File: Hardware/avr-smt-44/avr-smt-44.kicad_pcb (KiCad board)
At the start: 2 copper layers, 25.4 x 72.4 mm, 20 parts, among them J1 AVR-ISP-6, SW1 SW_Push, U1 ATtiny84A-SS

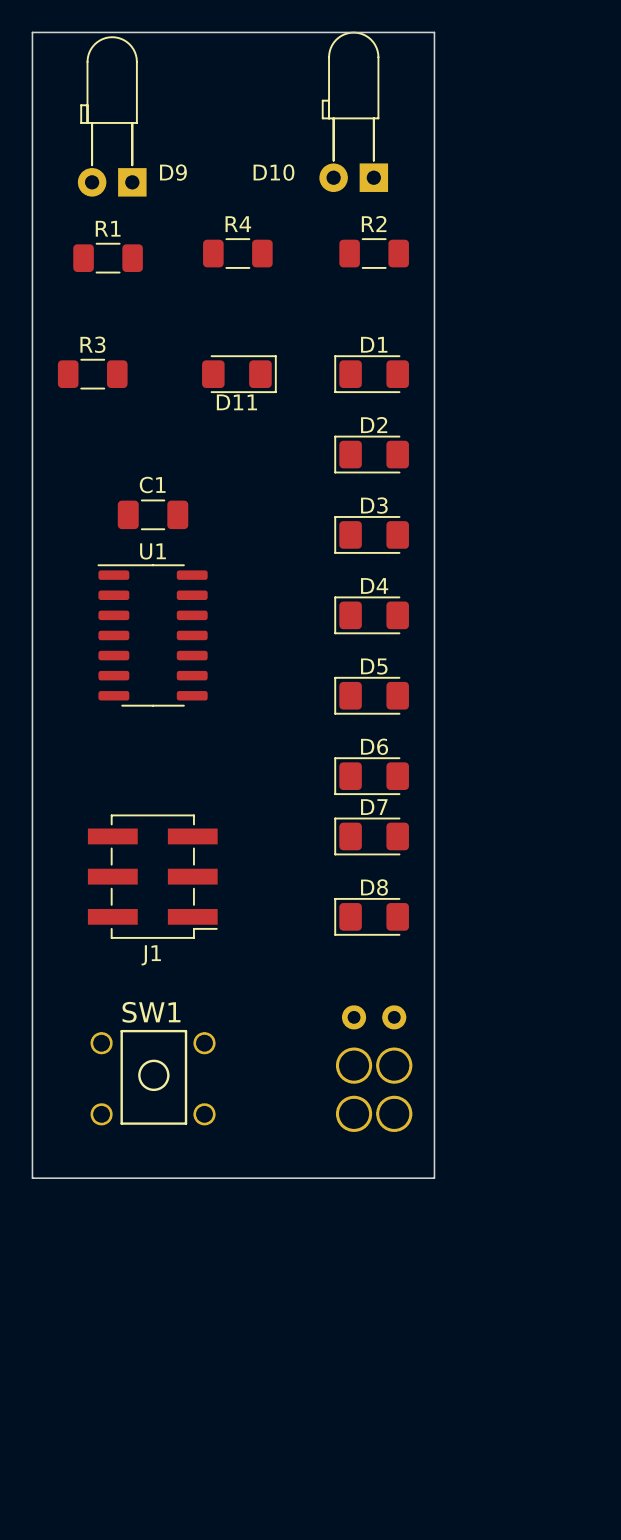
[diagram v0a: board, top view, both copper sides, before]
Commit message: Add series R, re-place
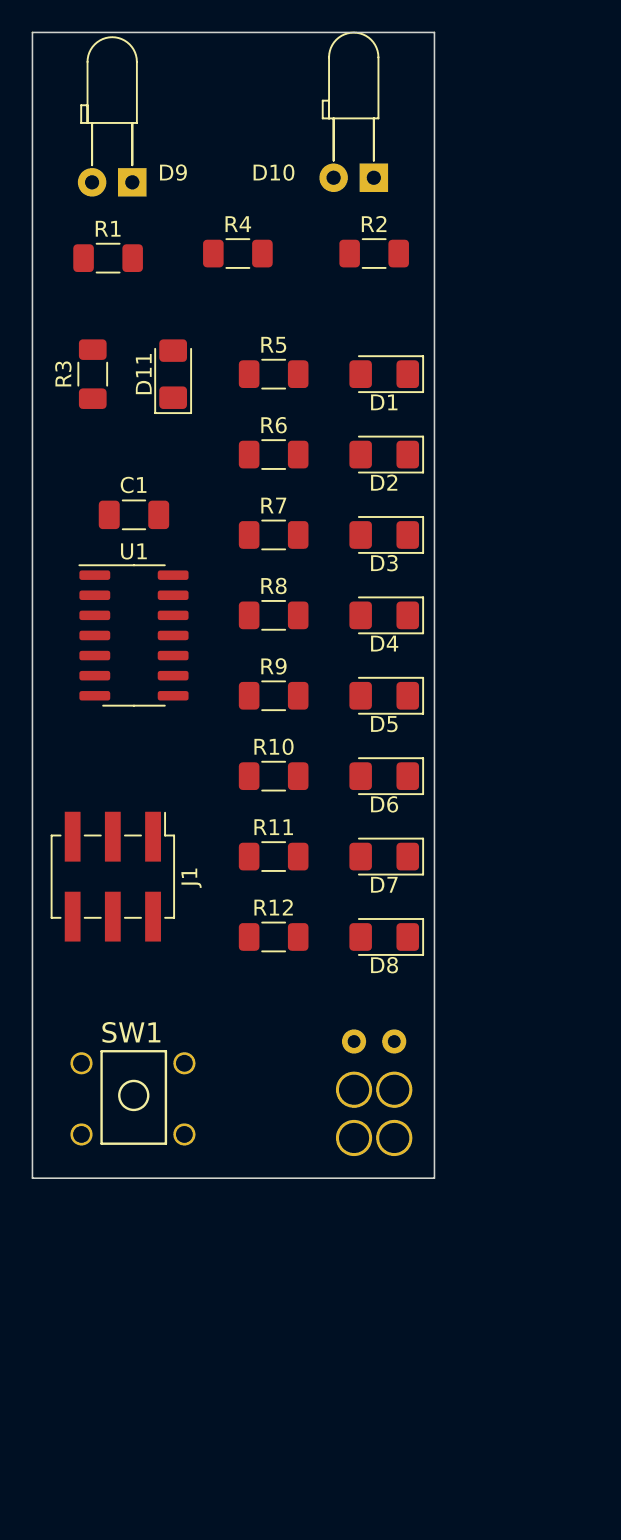
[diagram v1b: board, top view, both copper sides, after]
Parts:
- added R10: 330, Resistor_SMD:R_1206_3216Metric_Pad1.30x1.75mm_HandSolder, F.Cu at (167.6, 102.9)
- added R11: 330, Resistor_SMD:R_1206_3216Metric_Pad1.30x1.75mm_HandSolder, F.Cu at (167.6, 108.0)
- added R12: 330, Resistor_SMD:R_1206_3216Metric_Pad1.30x1.75mm_HandSolder, F.Cu at (167.6, 113.0)
- added R5: 330, Resistor_SMD:R_1206_3216Metric_Pad1.30x1.75mm_HandSolder, F.Cu at (167.6, 77.5)
- added R6: 330, Resistor_SMD:R_1206_3216Metric_Pad1.30x1.75mm_HandSolder, F.Cu at (167.6, 82.5)
- added R7: 330, Resistor_SMD:R_1206_3216Metric_Pad1.30x1.75mm_HandSolder, F.Cu at (167.6, 87.6)
- added R8: 330, Resistor_SMD:R_1206_3216Metric_Pad1.30x1.75mm_HandSolder, F.Cu at (167.6, 92.7)
- added R9: 330, Resistor_SMD:R_1206_3216Metric_Pad1.30x1.75mm_HandSolder, F.Cu at (167.6, 97.8)
- moved D11 4.03 mm to (161.3, 77.5), turned to 90 degrees
- moved J1 2.53 mm to (157.5, 109.2), turned to -90 degrees
- moved SW1 1.80 mm to (155.5, 121.0)
- moved BT1 1.52 mm to (174.0, 119.6)
- moved D7 1.42 mm to (174.6, 108.0), turned to 180 degrees
- moved D8 1.42 mm to (174.6, 113.0), turned to 180 degrees
- moved C1 1.21 mm to (158.8, 86.4)
- moved U1 1.21 mm to (158.8, 94.0)
- moved D1 0.63 mm to (174.6, 77.5), turned to 180 degrees
- moved D2 0.63 mm to (174.6, 82.5), turned to 180 degrees
- moved D3 0.63 mm to (174.6, 87.6), turned to 180 degrees
- moved D4 0.63 mm to (174.6, 92.7), turned to 180 degrees
- moved D5 0.63 mm to (174.6, 97.8), turned to 180 degrees
- moved D6 0.63 mm to (174.6, 102.9), turned to 180 degrees
- turned R3 to 90 degrees
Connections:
- U1 pad 10: Net-(D4-A) -> Net-(U1-PA3)
- U1 pad 11: Net-(D3-A) -> Net-(U1-PA2)
- U1 pad 12: Net-(D2-A) -> Net-(U1-PA1)
- U1 pad 13: Net-(D1-A) -> Net-(U1-AREF/PA0)
- U1 pad 2: Net-(D6-A) -> Net-(U1-XTAL1/PB0)
- U1 pad 3: Net-(D7-A) -> Net-(U1-XTAL2/PB1)
- U1 pad 5: Net-(D8-A) -> Net-(U1-PB2)
- U1 pad 6: Net-(D5-A) -> Net-(U1-PA7)

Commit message: V5 for submit
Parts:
- added N1: Housing, rhett_logo:rhett_logo, B.Cu at (165.1, 70.5)
- added TP1: TestPoint, TestPoint:TestPoint_Loop_D3.80mm_Drill2.0mm, F.Cu at (165.1, 59.1)
- added TP2: TestPoint, TestPoint:TestPoint_Loop_D3.80mm_Drill2.0mm, F.Cu at (167.0, 122.6)
- moved R1 1.03 mm to (156.2, 70.5), turned to 90 degrees
- moved R2 0.90 mm to (173.4, 70.5), turned to 90 degrees
- moved R4 0.69 mm to (165.1, 70.5), turned to -90 degrees
- turned D11 to -90 degrees
- turned R3 to -90 degrees
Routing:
- net /SCL: track 0.00 -> 62.8 mm, vias 0 -> 4
- net /MOSI: track 0.00 -> 57.5 mm, vias 0 -> 3
- net /nRESET: track 0.00 -> 51.6 mm, vias 0 -> 3
- net Net-(U1-PB2): track 0.00 -> 35.0 mm, vias 0 -> 2
- net /MISO: track 0.00 -> 27.9 mm, vias 0 -> 2
- net Net-(U1-XTAL2/PB1): track 0.00 -> 25.0 mm, vias 0 -> 4
- net Net-(U1-XTAL1/PB0): track 0.00 -> 21.6 mm, vias 0 -> 2
- net Net-(U1-AREF/PA0): track 0.00 -> 18.6 mm, vias 0 -> 2
- net GND: track 0.00 -> 16.3 mm, vias 0 -> 12
- net Net-(U1-PA1): track 0.00 -> 15.5 mm, vias 0 -> 2
- net Net-(U1-PA7): track 0.00 -> 13.5 mm, vias 0 -> 2
- net Net-(U1-PA2): track 0.00 -> 11.0 mm, vias 0 -> 2
- net Net-(U1-PA3): track 0.00 -> 6.91 mm
- net Net-(D11-A): track 0.00 -> 5.11 mm
- net Net-(D8-A): track 0.00 -> 3.95 mm
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- added copper zone on B.Cu, net GND
- added copper zone on F.Cu, net VCC
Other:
- board text added: "*1"
- board text added: "1"
- board text added: "AVR SMT V5"
- board text added: "Blinky POV"
- board text added: "Boston University EPIC"
- board text added: "Clock"
- board text added: "Data"

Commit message: assembly docs
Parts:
- added G***: LOGO, rhett_logo:rhett_logo, F.Cu at (182.3, 141.3)
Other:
- board text added: "# Reference Qty Value CatNo 1 BT1 1 Battery 1568-1408-ND 2 C1 1 0.1uF 399-C1206C104K3RAC7800CT-ND 3 D1, D2, D3, D4, D5, D6, D7, D8 8 LED 3147-T1341USD-30C000112U1930CT-ND 4 D9, D10 2 D_Photo 751-1057-ND 5 D11 1 LED Green 160-1169-1-ND 6 J1 1 AVR-ISP-6 10129383-906002BLF-ND 7 R1, R2, R4 3 10k 311-10KERCT-ND 8 R3 1 750 311-750ERCT-ND 9 R5, R6, R7, R8, R9, R10, R11, 8 330 311-330ERCT-ND 10 SW1 1 SW_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"
- board text added: "ASSEMBLY"
- board text added: "Suggested installation order: U1 R1-R12 D1-D8 (double check orientation!) SW1, D9, D10"

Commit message: instructions
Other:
- board text added: "Suggested installation order: U1 R1-R12 D1-D8 (double check orientation!) SW1, D9, D10 J1 Battery (note wire colors!)"
- board text removed: "Suggested installation order: U1 R1-R12 D1-D8 (double check orientation!) SW1, D9, D10"
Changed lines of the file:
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@@
     )
   )
-  (gr_text "Suggested installation order:\n\nU1\nR1-R12\nD1-D8    (double check orientation!)\nSW1, D9, D10\n" (at 22.1 128.7) (layer "User.3")
+  (gr_text "Suggested installation order:\n\nU1\nR1-R12\nD1-D8    (double check orientation!)\nSW1, D9, D10\nJ1\nBattery (note wire colors!)\n" (at 22.1 128.7) (layer "User.3")
     (effects (font (size 1.524 1.524) (thickness 0.1524)) (justify left bottom))
   )

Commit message: V5.1 PCB, notes
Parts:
- removed G***: LOGO, rhett_logo:rhett_logo
- J1: footprint Connector_PinHeader_2.54mm:PinHeader_2x03_P2.54mm_Vertical_SMD -> Connector_PinHeader_2.54mm:PinHeader_2x03_P2.54mm_Vertical
- moved J1 2.97 mm to (160.4, 108.7)
- moved C1 1.27 mm to (158.7, 85.1)
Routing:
- net /MISO: track 27.9 -> 32.4 mm
- net /SCL: track 62.8 -> 64.9 mm
- net /nRESET: track 51.6 -> 53.7 mm
- net GND: track 16.3 -> 18.0 mm, vias 12 -> 11
- net /MOSI: track 57.5 -> 59.2 mm
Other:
- board text added: "AVR SMT V5.1"
- board text removed: "AVR SMT V5"
